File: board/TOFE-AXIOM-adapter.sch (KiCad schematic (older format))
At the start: 8 parts, among them CN1 C, U1 24AA01/24LC01B

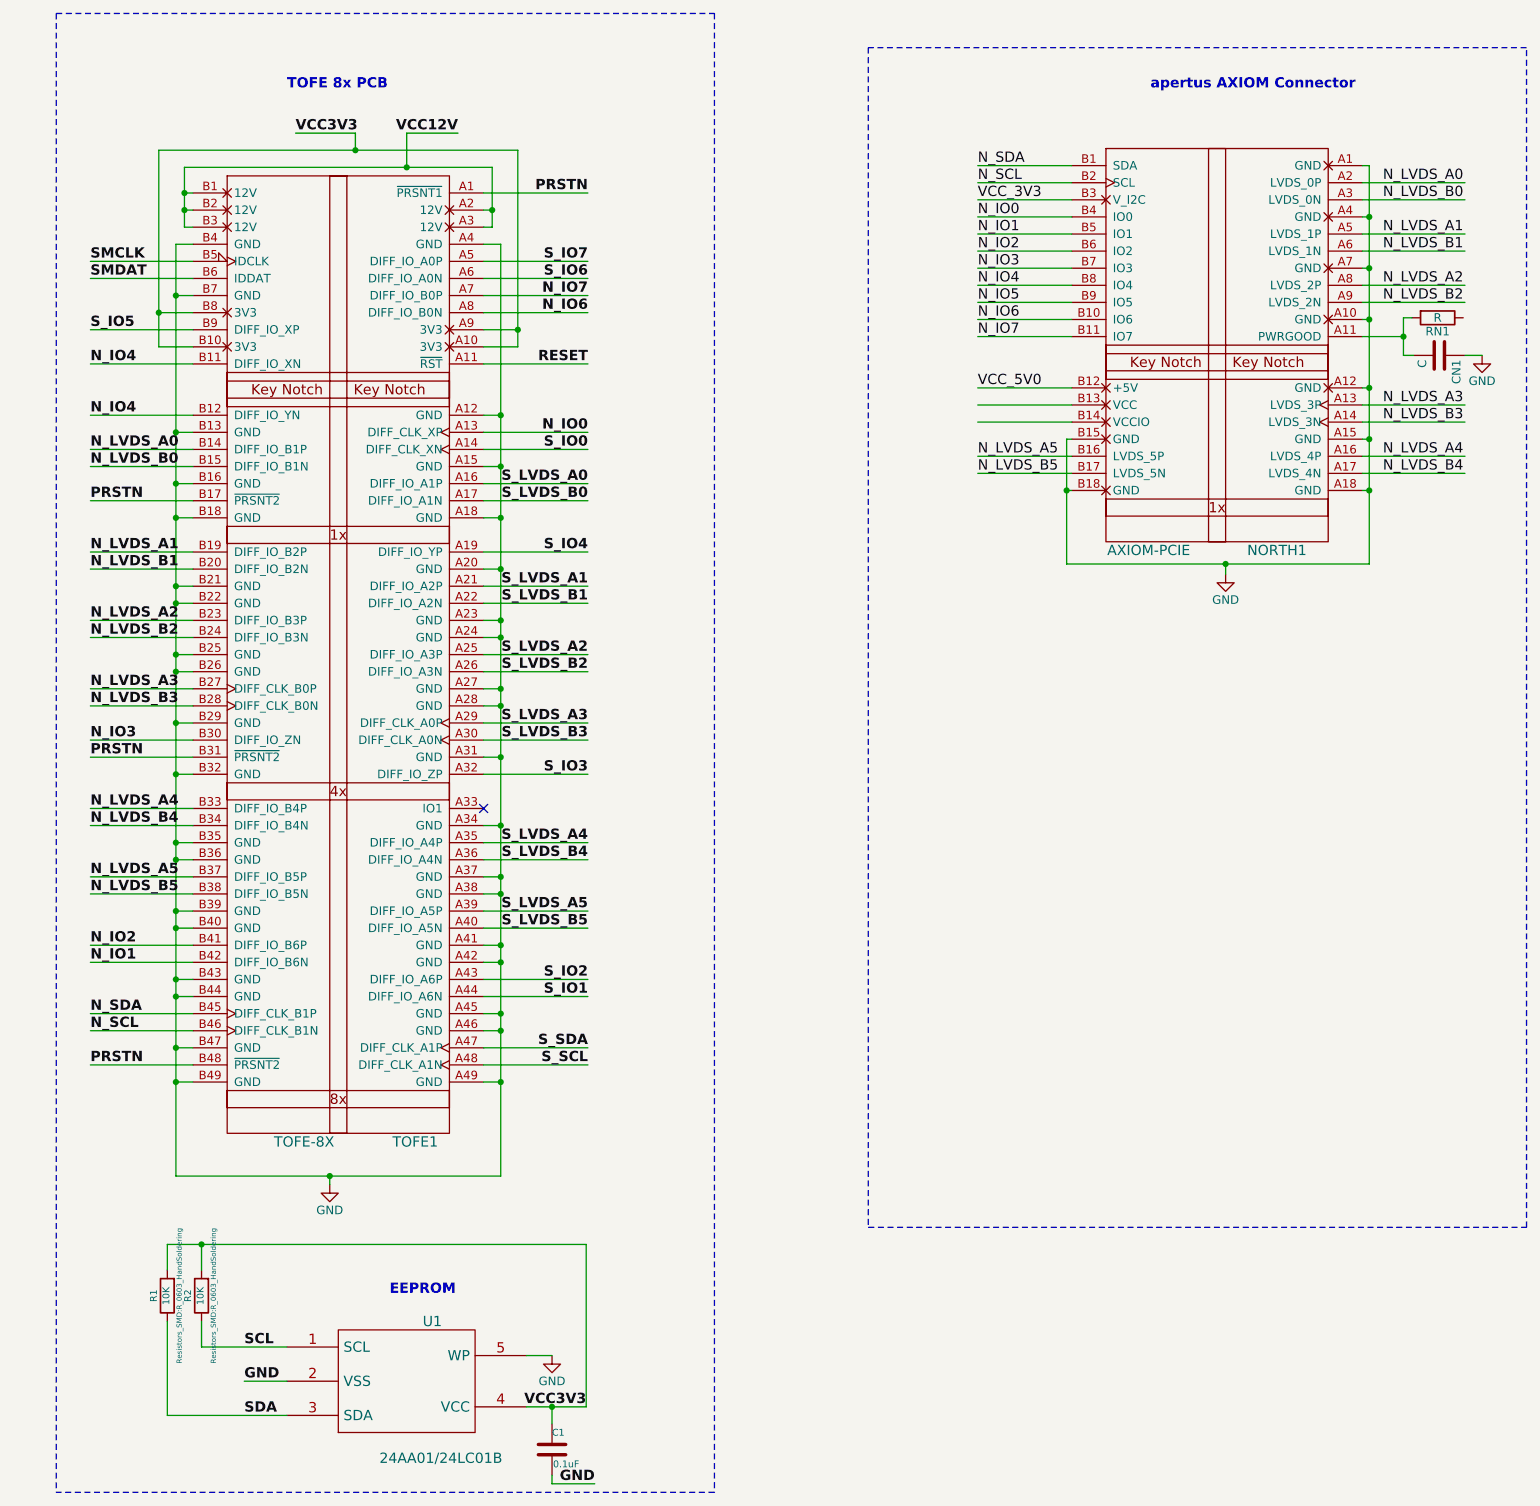
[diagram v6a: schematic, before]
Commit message: Fixing the diff pairs.
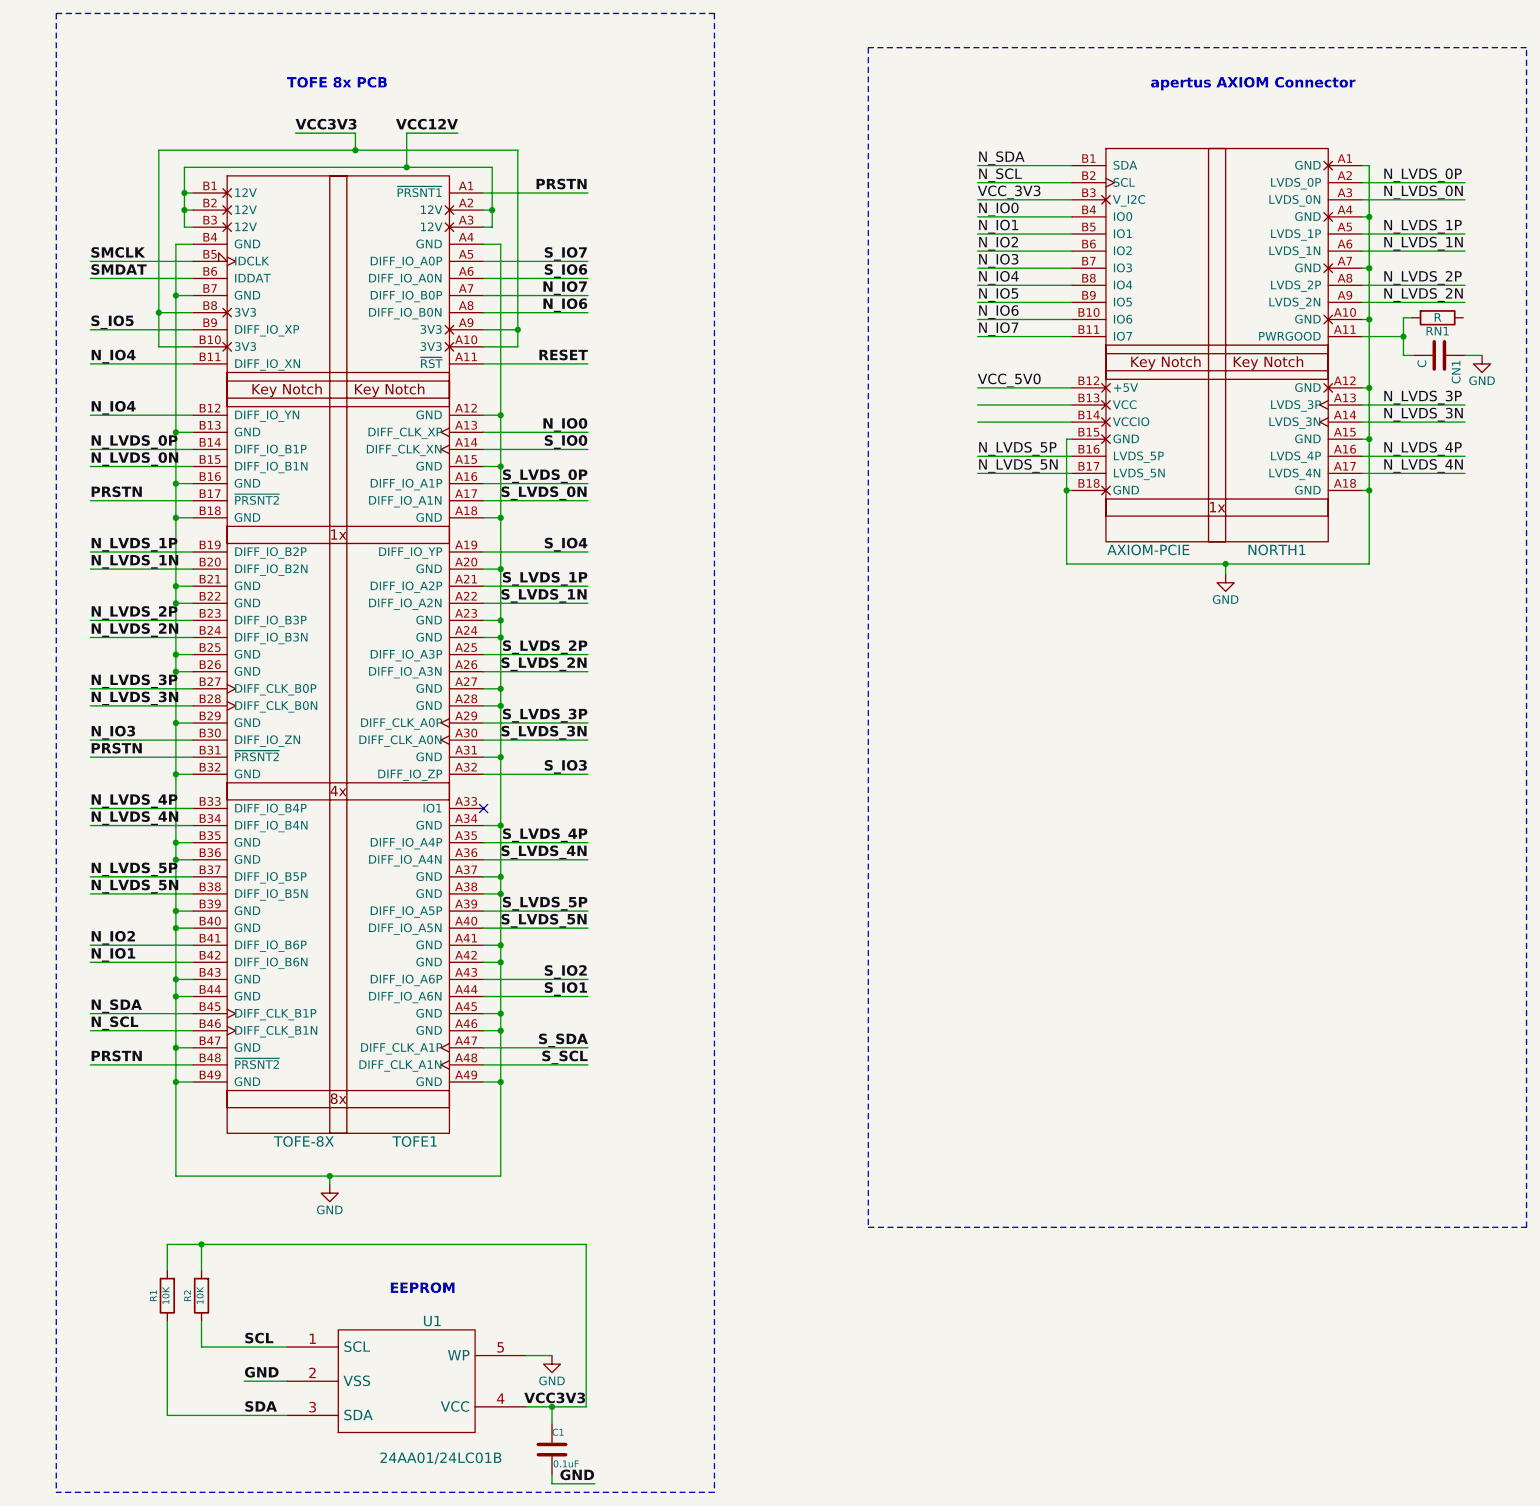
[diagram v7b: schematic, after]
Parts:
- C1: footprint (none) -> Capacitors_SMD:C_1206_HandSoldering
- U1: footprint (none) -> TO_SOT_Packages_SMD:SOT-23-5
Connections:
- net labels added: N_LVDS_0N, N_LVDS_0P, N_LVDS_1N, N_LVDS_1P, N_LVDS_2N, N_LVDS_2P, N_LVDS_3N, N_LVDS_3P, N_LVDS_4N, N_LVDS_4P, N_LVDS_5N, N_LVDS_5P, S_LVDS_0N, S_LVDS_0P, S_LVDS_1N, S_LVDS_1P, S_LVDS_2N, S_LVDS_2P, S_LVDS_3N, S_LVDS_3P, S_LVDS_4N, S_LVDS_4P, S_LVDS_5N, S_LVDS_5P
- net labels removed: N_LVDS_A0, N_LVDS_A1, N_LVDS_A2, N_LVDS_A3, N_LVDS_A4, N_LVDS_A5, N_LVDS_B0, N_LVDS_B1, N_LVDS_B2, N_LVDS_B3, N_LVDS_B4, N_LVDS_B5, S_LVDS_A0, S_LVDS_A1, S_LVDS_A2, S_LVDS_A3, S_LVDS_A4, S_LVDS_A5, S_LVDS_B0, S_LVDS_B1, S_LVDS_B2, S_LVDS_B3, S_LVDS_B4, S_LVDS_B5
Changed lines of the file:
@@
 S_IO0
 Text Label 6210 4250 2    60   ~ 12
-S_LVDS_A0
+S_LVDS_0P
 Text Label 6210 4350 2    60   ~ 12
-S_LVDS_B0
+S_LVDS_0N
 Text Label 6210 4850 2    60   ~ 12
-S_LVDS_A1
+S_LVDS_1P
 Text Label 6210 4950 2    60   ~ 12
-S_LVDS_B1
+S_LVDS_1N
 Text Label 6210 5250 2    60   ~ 12
-S_LVDS_A2
+S_LVDS_2P
 Text Label 6210 5350 2    60   ~ 12
-S_LVDS_B2
+S_LVDS_2N
 Text Label 6210 5650 2    60   ~ 12
-S_LVDS_A3
+S_LVDS_3P
 Text Label 6210 5750 2    60   ~ 12
-S_LVDS_B3
+S_LVDS_3N
 Text Label 6210 6350 2    60   ~ 12
-S_LVDS_A4
+S_LVDS_4P
 Text Label 4500 2200 0    60   ~ 12
 VCC3V3
@@
 TOFE 8x PCB
 Text Label 3300 4050 0    60   ~ 12
-N_LVDS_A0
+N_LVDS_0P
 Text Label 3300 4150 0    60   ~ 12
-N_LVDS_B0
+N_LVDS_0N
 Text Label 3300 4650 0    60   ~ 12
-N_LVDS_A1
+N_LVDS_1P
 Text Label 3300 4750 0    60   ~ 12
-N_LVDS_B1
+N_LVDS_1N
 Text Label 6210 4650 2    60   ~ 12
 S_IO4
 Text Label 3300 5150 0    60   ~ 12
-N_LVDS_B2
+N_LVDS_2N
 Text Label 3300 5050 0    60   ~ 12
-N_LVDS_A2
+N_LVDS_2P
 Text Label 3300 5550 0    60   ~ 12
-N_LVDS_B3
+N_LVDS_3N
 Text Label 3300 5450 0    60   ~ 12
-N_LVDS_A3
+N_LVDS_3P
 Text Label 3300 5750 0    60   ~ 12
 N_IO3
@@
 S_IO3
 Text Label 3300 6250 0    60   ~ 12
-N_LVDS_B4
+N_LVDS_4N
 Text Label 3300 6150 0    60   ~ 12
-N_LVDS_A4
+N_LVDS_4P
 Text Label 3300 6650 0    60   ~ 12
-N_LVDS_B5
+N_LVDS_5N
 Text Label 3300 6950 0    60   ~ 12
 N_IO2
 Text Label 6210 6750 2    60   ~ 12
-S_LVDS_A5
+S_LVDS_5P
 Text Label 6210 6850 2    60   ~ 12
-S_LVDS_B5
+S_LVDS_5N
 Text Label 6210 7250 2    60   ~ 12
 S_IO1
@@
 N_IO4
 Text Label 6210 6450 2    60   ~ 12
-S_LVDS_B4
+S_LVDS_4N
 Text Label 6210 3550 2    60   ~ 12
 RESET
 Text Label 3300 6550 0    60   ~ 12
-N_LVDS_A5
+N_LVDS_5P
 Text Label 6210 7650 2    60   ~ 12
 S_SCL
@@
 N_IO7
 Text Label 8490 4090 0    60   ~ 0
-N_LVDS_A5
+N_LVDS_5P
 Text Label 8490 4190 0    60   ~ 0
-N_LVDS_B5
+N_LVDS_5N
 Wire Wire Line
 	10740 3790 11340 3790
@@
 	10740 4190 11340 4190
 Text Label 10860 4090 0    60   ~ 0
-N_LVDS_A4
+N_LVDS_4P
 Text Label 10860 4190 0    60   ~ 0
-N_LVDS_B4
+N_LVDS_4N
 Text Label 10860 3890 0    60   ~ 0
-N_LVDS_B3
+N_LVDS_3N
 Text Label 10860 3790 0    60   ~ 0
-N_LVDS_A3
+N_LVDS_3P
 Wire Wire Line
 	10740 2790 11340 2790
@@
 	10740 3190 11340 3190
 Text Label 10860 3090 0    60   ~ 0
-N_LVDS_A2
+N_LVDS_2P
 Text Label 10860 3190 0    60   ~ 0
-N_LVDS_B2
+N_LVDS_2N
 Text Label 10860 2890 0    60   ~ 0
-N_LVDS_B1
+N_LVDS_1N
 Text Label 10860 2790 0    60   ~ 0
-N_LVDS_A1
+N_LVDS_1P
 Wire Wire Line
 	10740 2490 11340 2490
@@
 	10740 2590 11340 2590
 Text Label 10860 2590 0    60   ~ 0
-N_LVDS_B0
+N_LVDS_0N
 Text Label 10860 2490 0    60   ~ 0
-N_LVDS_A0
+N_LVDS_0P
 Wire Wire Line
 	10740 2390 10780 2390
@@
 F 0 "U1" H 5300 9850 60  0000 C CNN
 F 1 "24AA01/24LC01B" H 5350 9050 60  0000 C CNN
-F 2 "" H 5150 9500 60  0001 C CNN
+F 2 "TO_SOT_Packages_SMD:SOT-23-5" H 5150 9500 60  0001 C CNN
 F 3 "~" H 5150 9500 60  0000 C CNN
 	1    5150 9500
@@
 F 0 "R2" V 4030 9000 40  0000 C CNN
 F 1 "10K" V 3957 9001 40  0000 C CNN
-F 2 "Resistors_SMD:R_0603_HandSoldering" V 3880 9000 30  0000 C CNN
+F 2 "Resistors_SMD:R_0603_HandSoldering" V 3880 9000 30  0001 C CNN
 F 3 "~" H 3950 9000 30  0000 C CNN
 	1    3950 9000
@@
 F 0 "R1" V 3830 9000 40  0000 C CNN
 F 1 "10K" V 3757 9001 40  0000 C CNN
-F 2 "Resistors_SMD:R_0603_HandSoldering" V 3680 9000 30  0000 C CNN
+F 2 "Resistors_SMD:R_0603_HandSoldering" V 3680 9000 30  0001 C CNN
 F 3 "~" H 3750 9000 30  0000 C CNN
 	1    3750 9000
@@
 F 0 "C1" H 6000 10000 40  0000 L CNN
 F 1 "0.1uF" H 6006 9815 40  0000 L CNN
-F 2 "" H 6038 9750 30  0001 C CNN
+F 2 "Capacitors_SMD:C_1206_HandSoldering" H 6038 9750 30  0001 C CNN
 F 3 "~" H 6000 9900 60  0000 C CNN
 	1    6000 9900
@@
 	6000 10050 6000 10100
 $Comp
-L GND #PWR?
+L GND #PWR04
 U 1 1 56EBC6DB
 P 6000 9350
-F 0 "#PWR?" H 6000 9100 50  0001 C CNN
+F 0 "#PWR04" H 6000 9100 50  0001 C CNN
 F 1 "GND" H 6000 9200 50  0000 C CNN
 F 2 "" H 6000 9350 50  0000 C CNN

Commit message: Actually fixing the diff pairs.
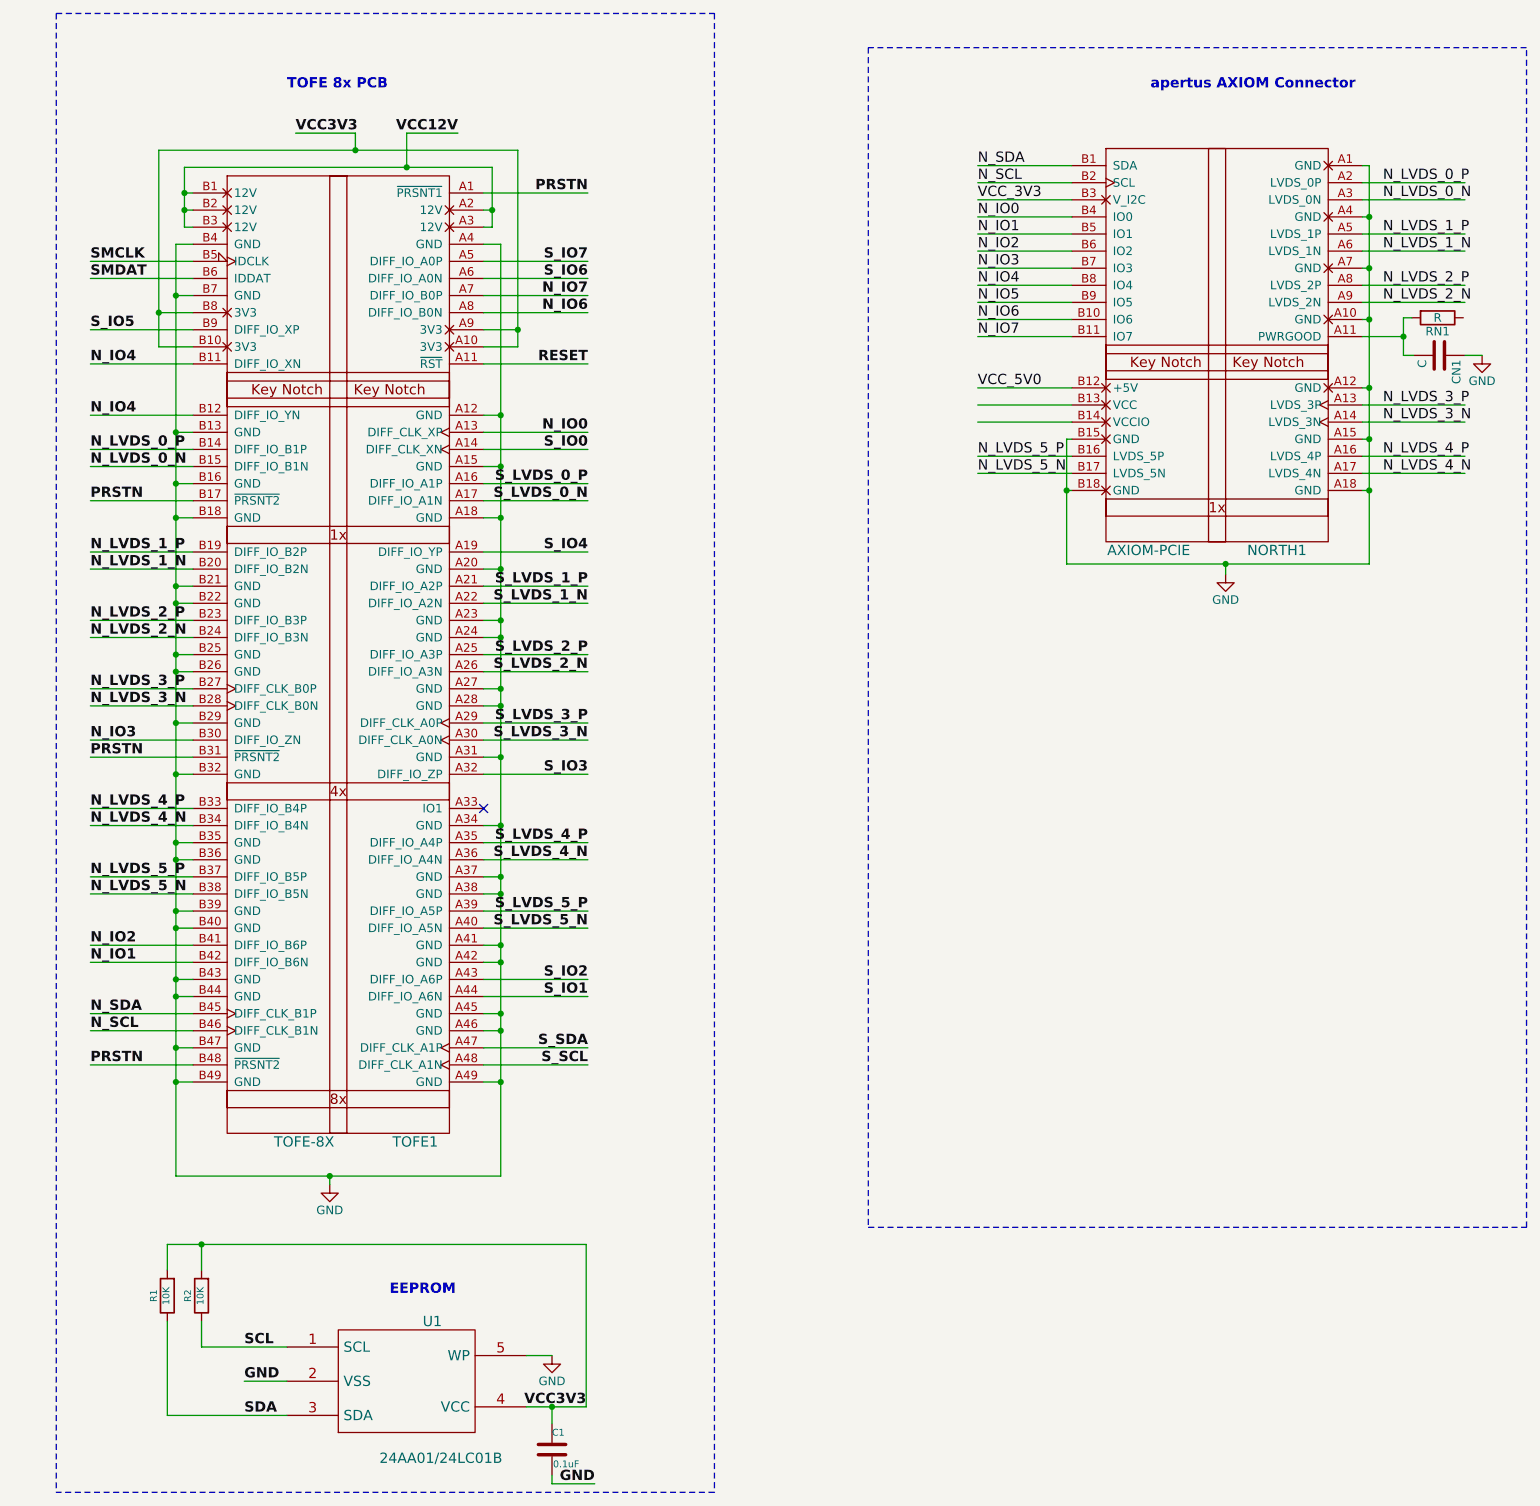
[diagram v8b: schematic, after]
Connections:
- net labels added: N_LVDS_0_N, N_LVDS_0_P, N_LVDS_1_N, N_LVDS_1_P, N_LVDS_2_N, N_LVDS_2_P, N_LVDS_3_N, N_LVDS_3_P, N_LVDS_4_N, N_LVDS_4_P, N_LVDS_5_N, N_LVDS_5_P, S_LVDS_0_N, S_LVDS_0_P, S_LVDS_1_N, S_LVDS_1_P, S_LVDS_2_N, S_LVDS_2_P, S_LVDS_3_N, S_LVDS_3_P, S_LVDS_4_N, S_LVDS_4_P, S_LVDS_5_N, S_LVDS_5_P
- net labels removed: N_LVDS_0N, N_LVDS_0P, N_LVDS_1N, N_LVDS_1P, N_LVDS_2N, N_LVDS_2P, N_LVDS_3N, N_LVDS_3P, N_LVDS_4N, N_LVDS_4P, N_LVDS_5N, N_LVDS_5P, S_LVDS_0N, S_LVDS_0P, S_LVDS_1N, S_LVDS_1P, S_LVDS_2N, S_LVDS_2P, S_LVDS_3N, S_LVDS_3P, S_LVDS_4N, S_LVDS_4P, S_LVDS_5N, S_LVDS_5P
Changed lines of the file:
@@
 S_IO0
 Text Label 6210 4250 2    60   ~ 12
-S_LVDS_0P
+S_LVDS_0_P
 Text Label 6210 4350 2    60   ~ 12
-S_LVDS_0N
+S_LVDS_0_N
 Text Label 6210 4850 2    60   ~ 12
-S_LVDS_1P
+S_LVDS_1_P
 Text Label 6210 4950 2    60   ~ 12
-S_LVDS_1N
+S_LVDS_1_N
 Text Label 6210 5250 2    60   ~ 12
-S_LVDS_2P
+S_LVDS_2_P
 Text Label 6210 5350 2    60   ~ 12
-S_LVDS_2N
+S_LVDS_2_N
 Text Label 6210 5650 2    60   ~ 12
-S_LVDS_3P
+S_LVDS_3_P
 Text Label 6210 5750 2    60   ~ 12
-S_LVDS_3N
+S_LVDS_3_N
 Text Label 6210 6350 2    60   ~ 12
-S_LVDS_4P
+S_LVDS_4_P
 Text Label 4500 2200 0    60   ~ 12
 VCC3V3
@@
 TOFE 8x PCB
 Text Label 3300 4050 0    60   ~ 12
-N_LVDS_0P
+N_LVDS_0_P
 Text Label 3300 4150 0    60   ~ 12
-N_LVDS_0N
+N_LVDS_0_N
 Text Label 3300 4650 0    60   ~ 12
-N_LVDS_1P
+N_LVDS_1_P
 Text Label 3300 4750 0    60   ~ 12
-N_LVDS_1N
+N_LVDS_1_N
 Text Label 6210 4650 2    60   ~ 12
 S_IO4
 Text Label 3300 5150 0    60   ~ 12
-N_LVDS_2N
+N_LVDS_2_N
 Text Label 3300 5050 0    60   ~ 12
-N_LVDS_2P
+N_LVDS_2_P
 Text Label 3300 5550 0    60   ~ 12
-N_LVDS_3N
+N_LVDS_3_N
 Text Label 3300 5450 0    60   ~ 12
-N_LVDS_3P
+N_LVDS_3_P
 Text Label 3300 5750 0    60   ~ 12
 N_IO3
@@
 S_IO3
 Text Label 3300 6250 0    60   ~ 12
-N_LVDS_4N
+N_LVDS_4_N
 Text Label 3300 6150 0    60   ~ 12
-N_LVDS_4P
+N_LVDS_4_P
 Text Label 3300 6650 0    60   ~ 12
-N_LVDS_5N
+N_LVDS_5_N
 Text Label 3300 6950 0    60   ~ 12
 N_IO2
 Text Label 6210 6750 2    60   ~ 12
-S_LVDS_5P
+S_LVDS_5_P
 Text Label 6210 6850 2    60   ~ 12
-S_LVDS_5N
+S_LVDS_5_N
 Text Label 6210 7250 2    60   ~ 12
 S_IO1
@@
 N_IO4
 Text Label 6210 6450 2    60   ~ 12
-S_LVDS_4N
+S_LVDS_4_N
 Text Label 6210 3550 2    60   ~ 12
 RESET
 Text Label 3300 6550 0    60   ~ 12
-N_LVDS_5P
+N_LVDS_5_P
 Text Label 6210 7650 2    60   ~ 12
 S_SCL
@@
 N_IO7
 Text Label 8490 4090 0    60   ~ 0
-N_LVDS_5P
+N_LVDS_5_P
 Text Label 8490 4190 0    60   ~ 0
-N_LVDS_5N
+N_LVDS_5_N
 Wire Wire Line
 	10740 3790 11340 3790
@@
 	10740 4190 11340 4190
 Text Label 10860 4090 0    60   ~ 0
-N_LVDS_4P
+N_LVDS_4_P
 Text Label 10860 4190 0    60   ~ 0
-N_LVDS_4N
+N_LVDS_4_N
 Text Label 10860 3890 0    60   ~ 0
-N_LVDS_3N
+N_LVDS_3_N
 Text Label 10860 3790 0    60   ~ 0
-N_LVDS_3P
+N_LVDS_3_P
 Wire Wire Line
 	10740 2790 11340 2790
@@
 	10740 3190 11340 3190
 Text Label 10860 3090 0    60   ~ 0
-N_LVDS_2P
+N_LVDS_2_P
 Text Label 10860 3190 0    60   ~ 0
-N_LVDS_2N
+N_LVDS_2_N
 Text Label 10860 2890 0    60   ~ 0
-N_LVDS_1N
+N_LVDS_1_N
 Text Label 10860 2790 0    60   ~ 0
-N_LVDS_1P
+N_LVDS_1_P
 Wire Wire Line
 	10740 2490 11340 2490
@@
 	10740 2590 11340 2590
 Text Label 10860 2590 0    60   ~ 0
-N_LVDS_0N
+N_LVDS_0_N
 Text Label 10860 2490 0    60   ~ 0
-N_LVDS_0P
+N_LVDS_0_P
 Wire Wire Line
 	10740 2390 10780 2390
